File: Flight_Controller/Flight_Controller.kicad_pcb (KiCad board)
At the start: 4 copper layers, 41.8 x 55.5 mm, 123 parts, among them IC1 ICM-20689, J1 USB_C_Receptacle_USB2.0_16P, J2 SM08B-SRSS-TB, J3 SM04B-SRSS-TB, J4 SM06B-SRSS-TBLFSN, J5 SM03B-SRSS-TB, Q1 AO3400A, SW1 SW_Push, U1 NO, U11 ESD224DQA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

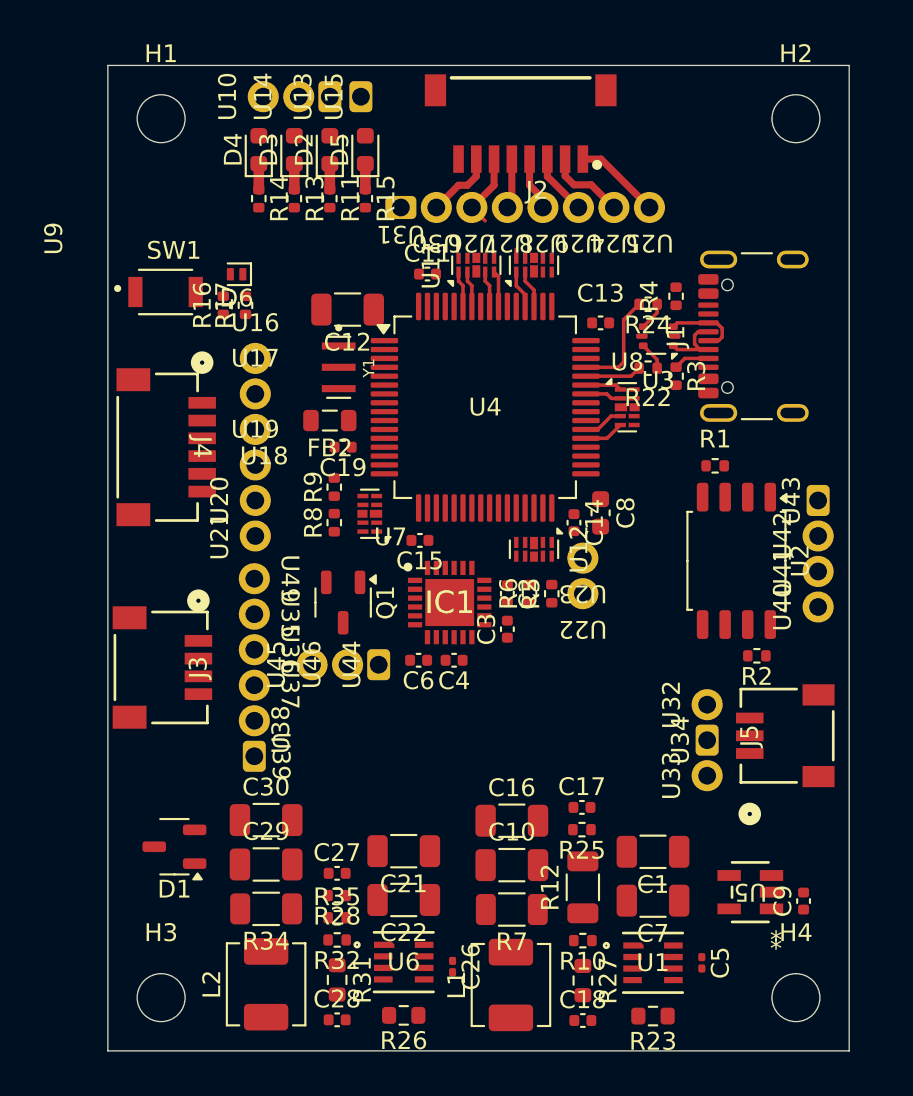
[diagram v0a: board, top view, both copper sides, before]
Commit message: Primer Ruteo, capas externas
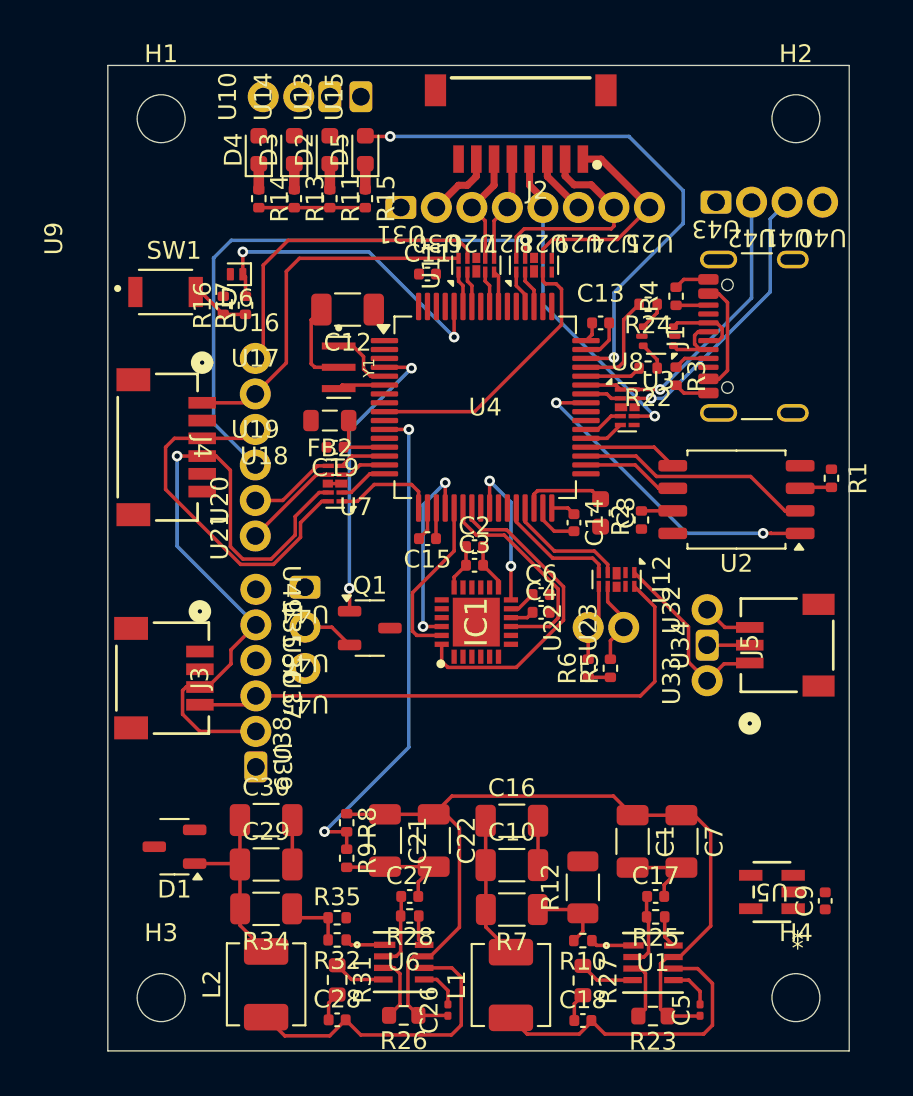
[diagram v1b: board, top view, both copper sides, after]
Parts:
- moved U40 22.8 mm to (210.8, 74.2), turned to 180 degrees
- moved R9 20.9 mm to (183.9, 111.2), turned to -90 degrees
- moved U41 20.9 mm to (208.8, 74.2), turned to 180 degrees
- moved U42 19.2 mm to (206.8, 74.2), turned to 180 degrees
- moved U43 17.8 mm to (204.8, 74.2), turned to 180 degrees
- moved R8 16.9 mm to (183.9, 109.2), turned to -90 degrees
- moved R2 10.0 mm to (200.6, 92.1), turned to 90 degrees
- moved C6 7.83 mm to (194.9, 96.3), turned to 0 degrees
- moved R1 6.59 mm to (211.2, 89.8), turned to -90 degrees
- moved C17 6.51 mm to (201.3, 113.3)
- moved R25 6.43 mm to (201.3, 114.5)
- moved U44 6.02 mm to (181.6, 95.9), turned to 180 degrees
- moved C4 5.59 mm to (194.9, 97.3), turned to 0 degrees
- moved U32 5.35 mm to (204.2, 97.2)
- moved U33 5.35 mm to (204.2, 101.2)
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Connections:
- U12 pad 1: /I2C_SDA_IN -> /VIDEO_IN
- U12 pad 10: /I2C_SDA_OUT -> /VIDEO_OUT
- U12 pad 2: /I2C_SCL_IN -> unconnected-(U12-Pad2)
- U12 pad 4: /ADC_CURR_IN -> /I2C_SDA_IN
- U12 pad 5: /VIDEO_IN -> /I2C_SCL_IN
- U12 pad 6: /VIDEO_OUT -> /I2C_SCL_OUT
- U12 pad 7: /ADC_CURR_OUT -> /I2C_SDA_OUT
- U12 pad 9: /I2C_SCL_OUT -> unconnected-(U12-Pad9)
- U9 pad 4: unconnected-(U9-Pad4) -> /ADC_CURR_IN
- U9 pad 7: unconnected-(U9-Pad7) -> /ADC_CURR_OUT
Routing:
- net +VLIPO: track 3.95 -> 56.7 mm
- net GND: track 0.00 -> 51.0 mm
- net /UART2_TX_OUT: track 0.00 -> 38.9 mm, vias 0 -> 1
- net /VIDEO_OUT: track 0.00 -> 32.0 mm
- net /LED0: track 0.00 -> 31.8 mm, vias 0 -> 2
- net /UART3_TX_OUT: track 0.00 -> 31.6 mm, vias 0 -> 1
- net /ADC_VBAT: track 0.00 -> 28.2 mm, vias 0 -> 2
- net /UART1_RX_OUT: track 0.00 -> 20.8 mm
- net /UART2_RX_OUT: track 0.00 -> 20.7 mm
- net /CS_FLASH: track 0.00 -> 18.5 mm, vias 0 -> 2
- net /SPI1_SDI: track 0.00 -> 18.3 mm
- net /UART1_TX_OUT: track 0.00 -> 18.2 mm
- net /BOOT0: track 0.00 -> 18.2 mm, vias 0 -> 2
- net Net-(U1-SW): track 0.00 -> 17.5 mm
- net Net-(U6-SW): track 0.00 -> 17.4 mm
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
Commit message: Correccion ruteo, capa GND
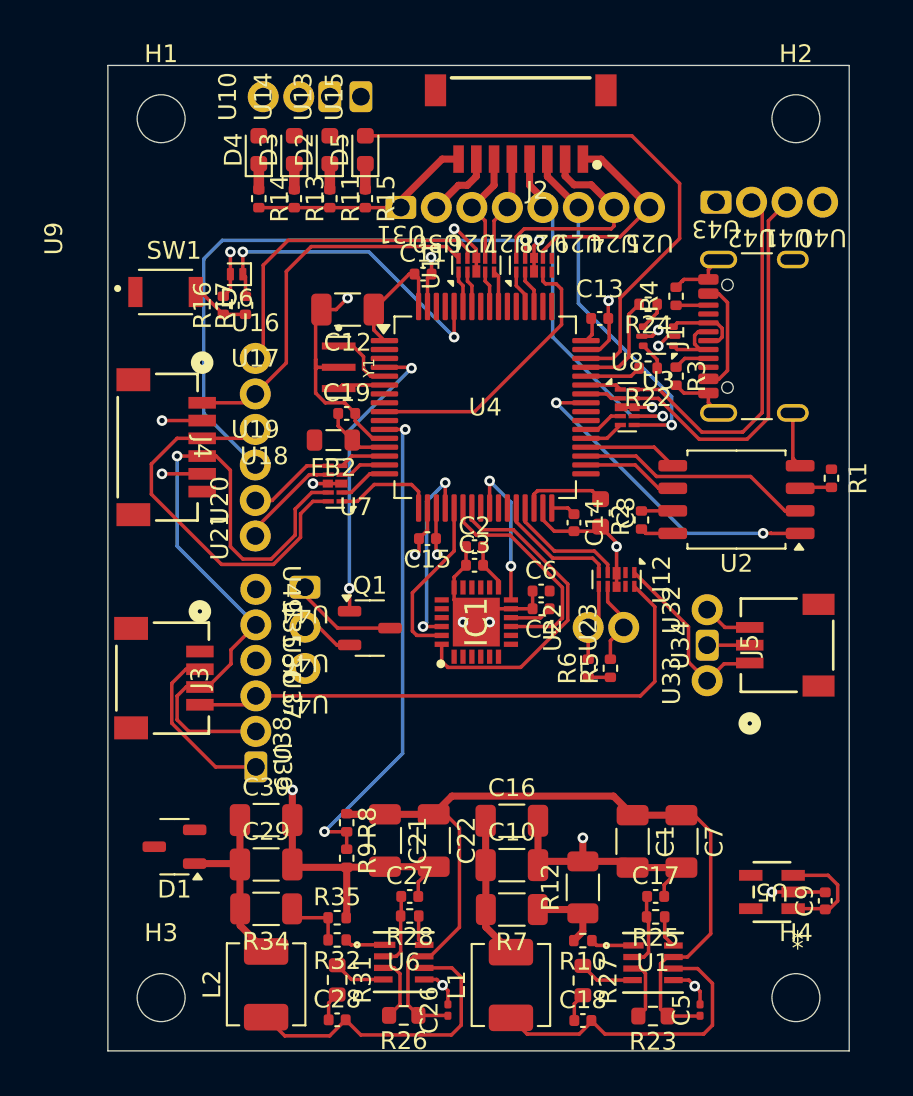
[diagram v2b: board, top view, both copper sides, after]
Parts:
- moved C19 2.01 mm to (183.9, 86.1), turned to 0 degrees
- moved FB2 1.12 mm to (183.2, 87.6)
- moved C13 0.25 mm to (198.2, 80.8)
- moved C11 0.25 mm to (188.2, 78.2)
- moved C4 0.20 mm to (194.9, 97.1), turned to 180 degrees
- moved C6 0.20 mm to (194.9, 96.1)
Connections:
- J1 pad S1: unconnected-(J1-SHIELD-PadS1)_1 -> GND
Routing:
- net GND: track 51.0 -> 138.6 mm, vias 0 -> 20
- net /MOTOR4_OUT: track 3.45 -> 20.0 mm, vias 0 -> 1
- net /+3.3V: track 8.18 -> 18.0 mm, vias 0 -> 1
- net /UART5_RX_OUT: track 14.1 -> 20.8 mm, vias 1 -> 0
- net +5V: track 0.00 -> 6.35 mm
- net /UART5_TX_OUT: track 15.6 -> 21.6 mm, vias 1 -> 0
- net /MOTOR3_OUT: track 18.6 -> 20.2 mm
- net /UART2_RX_OUT: track 20.7 -> 22.2 mm
- net Net-(IC1-REGOUT): track 1.34 -> 2.44 mm
- net +5VBUS: track 6.39 -> 7.46 mm, vias 0 -> 1
- net /UART2_TX_OUT: track 38.9 -> 39.8 mm
- net /UART3_TX_OUT: track 31.6 -> 32.4 mm
- net /SPI1_SDI: track 18.3 -> 18.9 mm
- net /UART1_RX_OUT: track 20.8 -> 21.4 mm
- net /SPI1_SDO: track 12.2 -> 12.7 mm
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
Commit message: Capa Potencia
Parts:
- moved R1 1.05 mm to (211.3, 90.8), turned to 90 degrees
- moved C9 0.29 mm to (210.6, 113.5)
- moved U5 0.29 mm to (207.6, 113.0)
- moved U10 0.26 mm to (179.2, 68.0)
- moved U13 0.26 mm to (183.0, 68.0)
- moved U14 0.26 mm to (181.2, 68.0)
- moved U15 0.26 mm to (184.8, 68.0)
- moved R2 0.10 mm to (200.6, 92.2)
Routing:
- net /+3.3V: track 18.0 -> 46.4 mm, vias 1 -> 12
- net +9V: track 10.8 -> 17.5 mm, vias 0 -> 2
- net +5V: track 6.35 -> 13.0 mm, vias 0 -> 4
- net Net-(U2-~{WP}/IO_{2}): track 1.79 -> 3.61 mm
- net +5VBAT: track 10.6 -> 12.3 mm, vias 0 -> 1
- net +VLIPO: track 56.9 -> 56.0 mm, vias 0 -> 2
- net +5VBUS: track 7.46 -> 6.93 mm, vias 1 -> 4
- added copper zone on In2.Cu, net +5V
- added copper zone on In2.Cu, net +5VBUS
- added copper zone on In2.Cu, net +9V
- added copper zone on In2.Cu, net +VLIPO
- added copper zone on In2.Cu, net /+3.3V
